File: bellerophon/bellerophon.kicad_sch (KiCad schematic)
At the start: 45 parts, among them Q1 ST3413A, Q2 SPP3414S23RG, Q3 SPP3414S23RG, U1 HT7350-A, U2 BNO055, U3 MPL3115A2, U4 Teensy4.0, U5 XTSD, Y1 32.768kHz

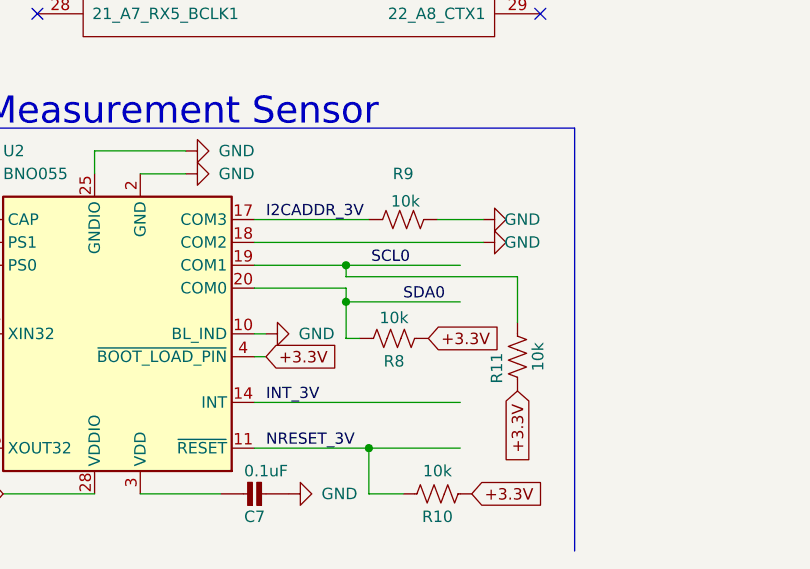
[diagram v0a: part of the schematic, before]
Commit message: remove interupt, reboot and I2Caddress connection from BNO055
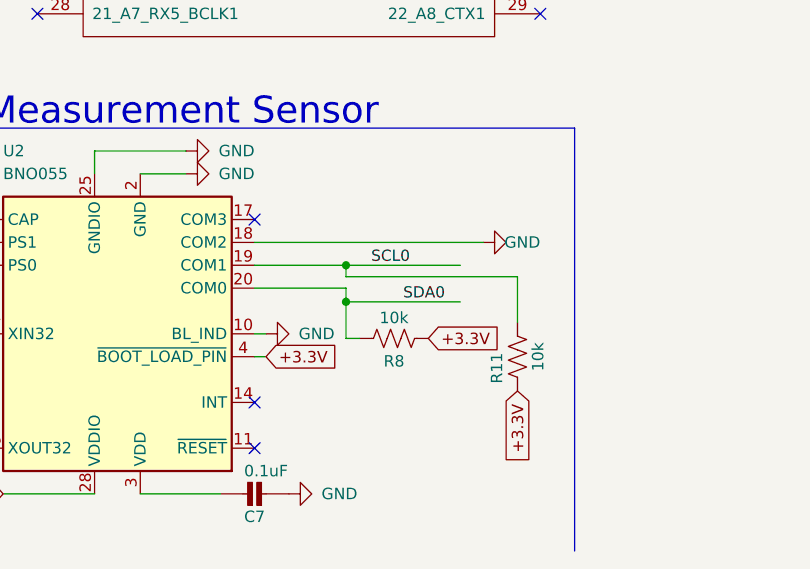
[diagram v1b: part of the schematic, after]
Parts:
- removed R10, R9: 10k, Resistor_SMD:R_0805_2012Metric, symbol Device:R_US
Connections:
- net I2CADDR_3V: no longer names the net of U2.17 (COM3)
- net INT_3V: no longer names the net of U2.14 (INT)
- net NRESET_3V: no longer names the net of U2.11 (~{RESET})
- no-connect marks 36 -> 39
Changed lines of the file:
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@@
   (junction (at 50.8 35.56) (diameter 0) (color 0 0 0 0)
-  )
-  (junction (at 153.67 186.69) (diameter 0) (color 0 0 0 0)
   )
   (junction (at 128.27 36.576) (diameter 0) (color 0 0 0 0)
@@
   (no_connect (at 116.84 85.09))
   (no_connect (at 152.908 36.576))
+  (no_connect (at 140.97 161.29))
+  (no_connect (at 140.97 186.69))
+  (no_connect (at 140.97 181.61))
   (wire (pts (xy 125.476 14.986) (xy 125.476 17.78))
     (stroke (width 0) (type default) (color 0 0 0 0))
@@
     (stroke (width 0) (type default) (color 0 0 0 0))
   )
-  (wire (pts (xy 153.67 186.69) (xy 163.83 186.69))
-    (stroke (width 0) (type default) (color 0 0 0 0))
-  )
   (wire (pts (xy 91.44 173.99) (xy 96.52 173.99))
     (stroke (width 0) (type default) (color 0 0 0 0))
@@
     (stroke (width 0) (type default) (color 0 0 0 0))
   )
-  (wire (pts (xy 140.97 181.61) (xy 163.83 181.61))
-    (stroke (width 0) (type default) (color 0 0 0 0))
-  )
   (wire (pts (xy 27.94 25.146) (xy 25.654 25.146))
     (stroke (width 0) (type default) (color 0 0 0 0))
@@
     (stroke (width 0) (type default) (color 0 0 0 0))
   )
-  (wire (pts (xy 140.97 161.29) (xy 153.67 161.29))
-    (stroke (width 0) (type default) (color 0 0 0 0))
-  )
   (wire (pts (xy 215.9 25.4) (xy 215.9 33.528))
     (stroke (width 0) (type default) (color 0 0 0 0))
@@
     (stroke (width 0) (type default) (color 0 0 0 0))
   )
-  (wire (pts (xy 157.48 191.77) (xy 153.67 191.77))
-    (stroke (width 0) (type default) (color 0 0 0 0))
-  )
   (wire (pts (xy 125.476 14.986) (xy 128.27 14.986))
     (stroke (width 0) (type default) (color 0 0 0 0))
@@
     (stroke (width 0) (type default) (color 0 0 0 0))
   )
-  (wire (pts (xy 153.67 186.69) (xy 153.67 191.77))
-    (stroke (width 0) (type default) (color 0 0 0 0))
-  )
   (wire (pts (xy 224.79 73.66) (xy 242.57 73.66))
     (stroke (width 0) (type default) (color 0 0 0 0))
@@
     (stroke (width 0) (type default) (color 0 0 0 0))
   )
-  (wire (pts (xy 161.29 161.29) (xy 166.37 161.29))
-    (stroke (width 0) (type default) (color 0 0 0 0))
-  )
   (wire (pts (xy 151.13 174.498) (xy 152.654 174.498))
     (stroke (width 0) (type default) (color 0 0 0 0))
@@
   )
   (wire (pts (xy 59.69 27.94) (xy 59.69 35.56))
-    (stroke (width 0) (type default) (color 0 0 0 0))
-  )
-  (wire (pts (xy 140.97 186.69) (xy 153.67 186.69))
     (stroke (width 0) (type default) (color 0 0 0 0))
   )
@@
     (effects (font (size 1.2446 1.2446)) (justify left bottom))
   )
-  (label "I2CADDR_3V" (at 142.24 161.29 0)
-    (effects (font (size 1.2446 1.2446)) (justify left bottom))
-  )
   (label "SCL1" (at 120.142 39.116 0)
     (effects (font (size 1.27 1.27)) (justify left bottom))
@@
     (effects (font (size 1.2446 1.2446)) (justify left bottom))
   )
-  (label "NRESET_3V" (at 142.24 186.69 0)
-    (effects (font (size 1.2446 1.2446)) (justify left bottom))
-  )
   (label "SCL0" (at 103.886 133.35 0)
     (effects (font (size 1.27 1.27)) (justify left bottom))
-  )
-  (label "INT_3V" (at 142.24 181.61 0)
-    (effects (font (size 1.2446 1.2446)) (justify left bottom))
   )
   (label "MISO" (at 111.76 102.87 0)
@@
     (property "Intersheet References" "${INTERSHEET_REFS}" (id 0) (at 100.6988 90.0906 0)
       (effects (font (size 1.27 1.27)) (justify right) hide)
-    )
-  )
-  (global_label "+3.3V" (shape input) (at 165.1 191.77 0) (fields_autoplaced)
-    (effects (font (size 1.27 1.27)) (justify left))
-    (property "Intersheet References" "${INTERSHEET_REFS}" (id 0) (at 173.1979 191.8494 0)
-      (effects (font (size 1.27 1.27)) (justify left) hide)
     )
   )
@@
     (pin "2")
   )
-  (symbol (lib_id "Device:R_US") (at 157.48 161.29 270) (unit 1)
-    (in_bom yes) (on_board yes)
-    (property "Reference" "R9" (id 0) (at 157.48 156.21 90))
-    (property "Value" "10k" (id 1) (at 157.734 159.258 90))
-    (property "Footprint" "Resistor_SMD:R_0805_2012Metric" (id 2) (at 157.226 162.306 90)
-      (effects (font (size 1.27 1.27)) hide)
-    )
-    (property "Datasheet" "https://au.rs-online.com/web/p/surface-mount-resistors/2232215" (id 3) (at 157.48 161.29 0)
-      (effects (font (size 1.27 1.27)) hide)
-    )
-    (pin "1")
-    (pin "2")
-  )
   (symbol (lib_id "power:GND") (at 111.252 36.576 0) (unit 1)
     (in_bom yes) (on_board yes) (fields_autoplaced)
@@
     (pin "2")
   )
-  (symbol (lib_id "Device:R_US") (at 161.29 191.77 90) (unit 1)
-    (in_bom yes) (on_board yes)
-    (property "Reference" "R10" (id 0) (at 161.29 194.31 90))
-    (property "Value" "10k" (id 1) (at 161.29 189.23 90))
-    (property "Footprint" "Resistor_SMD:R_0805_2012Metric" (id 2) (at 161.544 190.754 90)
-      (effects (font (size 1.27 1.27)) hide)
-    )
-    (property "Datasheet" "https://au.rs-online.com/web/p/surface-mount-resistors/2232215" (id 3) (at 161.29 191.77 0)
-      (effects (font (size 1.27 1.27)) hide)
-    )
-    (pin "1")
-    (pin "2")
-  )
   (symbol (lib_id "Connector:Screw_Terminal_01x04") (at 20.574 27.686 180) (unit 1)
     (in_bom yes) (on_board yes) (fields_autoplaced)
@@
     (pin "1")
     (pin "2")
-  )
-  (symbol (lib_id "power:GND") (at 166.37 161.29 90) (unit 1)
-    (in_bom yes) (on_board yes)
-    (property "Reference" "#PWR022" (id 0) (at 172.72 161.29 0)
-      (effects (font (size 1.27 1.27)) hide)
-    )
-    (property "Value" "GND" (id 1) (at 172.72 161.29 90)
-      (effects (font (size 1.27 1.27)) (justify left))
-    )
-    (property "Footprint" "" (id 2) (at 166.37 161.29 0)
-      (effects (font (size 1.27 1.27)) hide)
-    )
-    (property "Datasheet" "" (id 3) (at 166.37 161.29 0)
-      (effects (font (size 1.27 1.27)) hide)
-    )
-    (pin "1")
   )
   (symbol (lib_id "power:GND") (at 195.58 25.4 0) (unit 1)
@@
       (reference "#PWR021") (unit 1) (value "GND") (footprint "")
     )
-    (path "/a899ed8d-14d4-49cb-b248-1048b0c0d1f3"
-      (reference "#PWR022") (unit 1) (value "GND") (footprint "")
-    )
     (path "/bcc29a0a-e47f-40c2-a550-75601b8eed46"
       (reference "#PWR023") (unit 1) (value "GND") (footprint "")
@@
       (reference "R8") (unit 1) (value "10k") (footprint "Resistor_SMD:R_0805_2012Metric")
     )
-    (path "/8b01aadd-658d-4872-980a-1da80f58d537"
-      (reference "R9") (unit 1) (value "10k") (footprint "Resistor_SMD:R_0805_2012Metric")
-    )
-    (path "/a1d0c0db-ad94-426d-b766-9d627c31c08b"
-      (reference "R10") (unit 1) (value "10k") (footprint "Resistor_SMD:R_0805_2012Metric")
-    )
     (path "/00257695-cb44-46c1-a958-a3b7e278daeb"

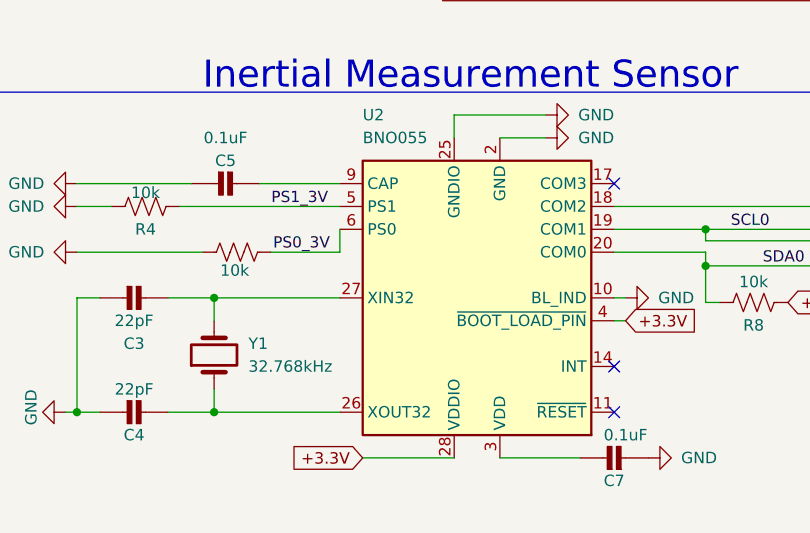
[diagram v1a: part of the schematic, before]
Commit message: finalized bno055 circuitry and placement
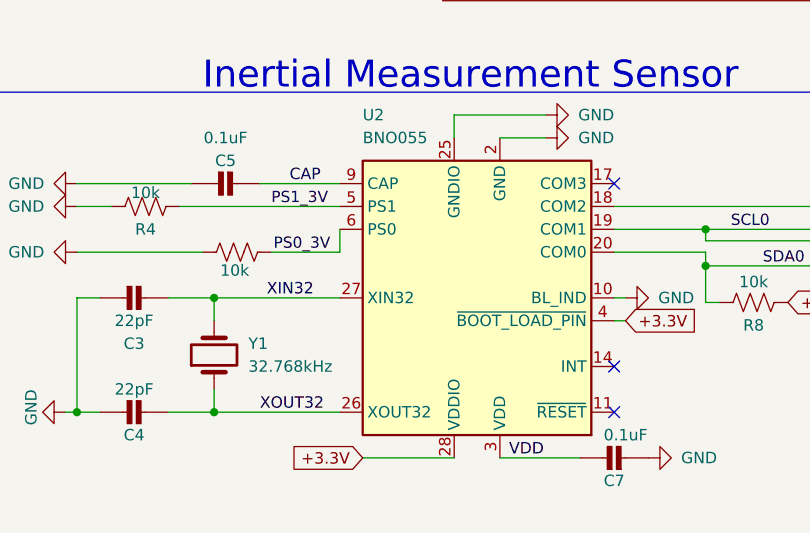
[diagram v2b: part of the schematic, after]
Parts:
- R11: footprint Resistor_SMD:R_1206_3216Metric_Pad1.30x1.75mm_HandSolder -> Resistor_SMD:R_0805_2012Metric
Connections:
- net PS0_3V: now also R5.1, U2.6 (PS0)
- net VDD: now reaches C7.1, U2.3 (VDD)
- net XOUT32: now reaches C4.1, U2.26 (XOUT32), Y1.1
- net XIN32: now reaches C3.1, U2.27 (XIN32), Y1.2
- net CAP: now reaches C5.1, U2.9 (CAP)

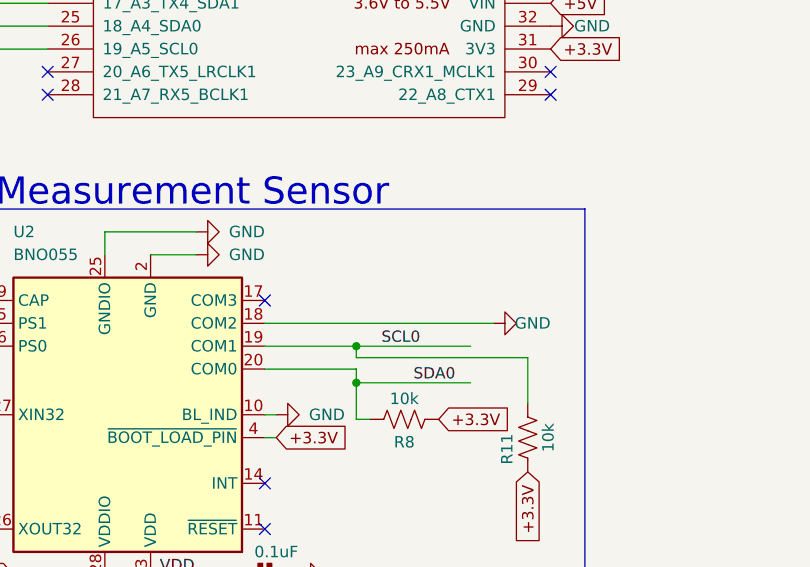
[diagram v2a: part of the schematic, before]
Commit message: add back i2cADDR pin for bno055
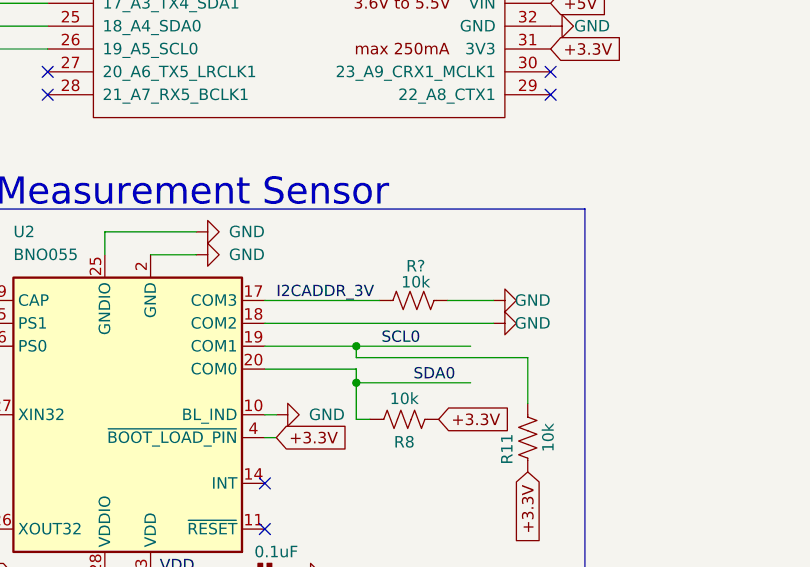
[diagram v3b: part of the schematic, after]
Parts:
- added R?: 10k, Resistor_SMD:R_0805_2012Metric, symbol Device:R_US
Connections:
- net GND: now also R?.1
- net I2CADDR_3V: now reaches U2.17 (COM3)
- net I2CADDR_3V: now also R?.2
- no-connect marks 39 -> 38
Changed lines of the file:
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@@
   (no_connect (at 116.84 85.09))
   (no_connect (at 152.908 36.576))
-  (no_connect (at 140.97 161.29))
   (no_connect (at 140.97 186.69))
   (no_connect (at 140.97 181.61))
@@
     (stroke (width 0) (type default) (color 0 0 0 0))
   )
+  (wire (pts (xy 161.29 161.29) (xy 166.37 161.29))
+    (stroke (width 0) (type default) (color 0 0 0 0))
+  )
   (wire (pts (xy 128.27 25.4) (xy 128.27 36.576))
     (stroke (width 0) (type default) (color 0 0 0 0))
@@
   )
   (wire (pts (xy 215.9 25.4) (xy 227.33 25.4))
+    (stroke (width 0) (type default) (color 0 0 0 0))
+  )
+  (wire (pts (xy 140.97 161.29) (xy 153.67 161.29))
     (stroke (width 0) (type default) (color 0 0 0 0))
   )
@@
   (label "SDA0" (at 103.886 130.81 0)
     (effects (font (size 1.27 1.27)) (justify left bottom))
+  )
+  (label "I2CADDR_3V" (at 142.24 161.29 0)
+    (effects (font (size 1.2446 1.2446)) (justify left bottom))
   )
   (label "SDA1" (at 120.142 36.576 0)
@@
     (pin "2")
   )
+  (symbol (lib_id "Device:R_US") (at 157.48 161.29 270) (unit 1)
+    (in_bom yes) (on_board yes)
+    (property "Reference" "R?" (id 0) (at 157.734 157.48 90))
+    (property "Value" "10k" (id 1) (at 157.734 159.258 90))
+    (property "Footprint" "Resistor_SMD:R_0805_2012Metric" (id 2) (at 157.226 162.306 90)
+      (effects (font (size 1.27 1.27)) hide)
+    )
+    (property "Datasheet" "https://au.rs-online.com/web/p/surface-mount-resistors/2232215" (id 3) (at 157.48 161.29 0)
+      (effects (font (size 1.27 1.27)) hide)
+    )
+    (pin "1")
+    (pin "2")
+  )
   (symbol (lib_id "Connector:Screw_Terminal_01x04") (at 20.574 27.686 180) (unit 1)
     (in_bom yes) (on_board yes) (fields_autoplaced)
@@
     )
     (property "Datasheet" "" (id 3) (at 172.72 130.81 0)
+      (effects (font (size 1.27 1.27)) hide)
+    )
+    (pin "1")
+  )
+  (symbol (lib_id "power:GND") (at 166.37 161.29 90) (unit 1)
+    (in_bom yes) (on_board yes)
+    (property "Reference" "#PWR?" (id 0) (at 172.72 161.29 0)
+      (effects (font (size 1.27 1.27)) hide)
+    )
+    (property "Value" "GND" (id 1) (at 172.72 161.29 90)
+      (effects (font (size 1.27 1.27)) (justify left))
+    )
+    (property "Footprint" "" (id 2) (at 166.37 161.29 0)
+      (effects (font (size 1.27 1.27)) hide)
+    )
+    (property "Datasheet" "" (id 3) (at 166.37 161.29 0)
       (effects (font (size 1.27 1.27)) hide)
     )
@@
       (reference "#PWR032") (unit 1) (value "GND") (footprint "")
     )
+    (path "/ed213b2a-574f-4509-a8a9-53ac25a6883e"
+      (reference "#PWR?") (unit 1) (value "GND") (footprint "")
+    )
     (path "/8a393ed2-cfe0-4f0f-9490-ab6f8e39e2cc"
       (reference "BZ1") (unit 1) (value "Buzzer") (footprint "Buzzer:PiezoBuzzer-PS1240")
@@
       (reference "R20") (unit 1) (value "49.9k") (footprint "Resistor_SMD:R_1206_3216Metric_Pad1.30x1.75mm_HandSolder")
     )
+    (path "/a62b7c54-0a9a-4c2b-9155-3ab5a75979d9"
+      (reference "R?") (unit 1) (value "10k") (footprint "Resistor_SMD:R_0805_2012Metric")
+    )
     (path "/a6785074-04ef-4659-a3ac-ebad7b1a7692"

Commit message: finalize MPL circuitry
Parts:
- gave numbers to parts that had none: 1
- renumbered C7 to C8, C8 to C9, R11 to R10, R12 to R11, R13 to R12, R14 to R13, R15 to R14, R16 to R15, R17 to R16, R18 to R17, R19 to R18, R20 to R19
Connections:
- net VDD is gone; now on net +3.3V: C8.1, U2.3 (VDD)
- net CAP1: now reaches C9.1, U3.2 (CAP)
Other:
- moved on the sheet: C9
